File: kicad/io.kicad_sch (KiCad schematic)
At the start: 12 parts, among them J2 UART, P1 Mini-DIN_6pins_ver3, U13 uSD adapter, U14 8259, U16 16550, U17 T6963C

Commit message: PS/2 with GAL - finally
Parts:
- removed R2: 10K, Resistor_THT:R_Axial_DIN0204_L3.6mm_D1.6mm_P7.62mm_Horizontal, symbol Device:R
- added BZ1: Buzzer, symbol Device:Buzzer
- added R2 (x2): 10K, Resistor_THT:R_Axial_DIN0204_L3.6mm_D1.6mm_P7.62mm_Horizontal, symbol Device:R
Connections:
- net GND: now also BZ1.2 (+), R2.1
- net INT1: now also U?.17 (PC3); no longer U?.14 (PC0)
- net MCB: now also U?.22 (PB4), R2.2; no longer U?.4 (PA0)
- net PS2CLK: now also U?.13 (PC4); no longer U?.16 (PC2)
- net PS2DATA: now also U?.4 (PA0); no longer U?.18 (PB0)
- net TIMERCLK: now also U?.18 (CLK2)
- net BUZEN: now reaches U?.16 (G2)
- net BUZEN: now also U?.18 (PB0)
- net BUZOUT: now reaches U?.17 (OUT2)
- net BUZOUT: now also R2.2
- new net: BZ1.1 (-), R2.1
- no-connect marks 42 -> 38
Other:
- note added: "Buzzer"
- note added: "IBF_{A}"
- note added: "INTR_{A}"
- note added: "IO"
- note added: "Port A control for mode 1 (strobed I/O)"
- note added: "Port B control for mode 1 (strobed I/O)"
- note added: "~{STB}_{A}"

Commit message: V0.3 WIP
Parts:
- added U20: ATF22V10, Package_DIP:DIP-24_W7.62mm_Socket, symbol my:ATF22V10
- BZ1: footprint (none) -> Buzzer_Beeper:Buzzer_TDK_PS1240P02BT_D12.2mm_H6.5mm
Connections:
- net +5V: now also U20.24 (VCC)
- net AD_{0}: now also U20.21 (O)
- net AD_{1}: now also U20.20 (O)
- net AD_{2}: now also U20.19 (O)
- net AD_{3}: now also U20.18 (O)
- net AD_{4}: now also U20.17 (O)
- net AD_{5}: now also U20.16 (O)
- net AD_{6}: now also U20.15 (O)
- net AD_{7}: now also U20.14 (O)
- net A_{0}: now also U20.3 (I)
- net GND: now also U20.12 (GND)
- net INT1: now also U20.23 (O); no longer U?.17 (PC3)
- net PS2CLK: now also U20.1 (CLK); no longer U?.13 (PC4)
- net PS2DATA: now also U20.2 (I); no longer U?.4 (PA0)
- net ~{RD}: now also U20.4 (I)
- net at U16.32 (~{RTS}): no longer U13.6 (~{CS})
- net at U16.33 (~{DTR}): no longer U13.5 (SCK)
- net at U16.34 (~{OUT1}): no longer U13.4 (MOSI)
- net at U16.36 (~{CTS}): no longer U13.3 (MISO)
- net at U?.11 (PC6): now also U13.6 (~{CS})
- net at U?.12 (PC5): now also U13.5 (SCK)
- net at U?.14 (PC0): now also U13.3 (MISO)
- net SPKREN: now reaches U?.19 (PB1)
- net BUZEN renamed T2GATE
- net BUZOUT renamed SPKROUT
- net SPKROUT: no longer U?.17 (OUT2)
- new net: U13.4 (MOSI), U?.13 (PC4)
- new net PS2~{EN}: U20.13 (I)
- new net T2OUT: U?.17 (OUT2)
- no-connect marks 38 -> 48
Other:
- note added: "Mode = 0 (basic)"
- note added: "Peripheral controller"
- note added: "Port A = N/C"
- note added: "Port B = 0 (OUT)"
- note added: "Port C (high) = 0 (OUT)"
- note added: "Port C (low) = 1 (IN)"
- note added: "Speaker"
- note removed: "0,1"
- note removed: "Buzzer"
- note removed: "IBF_{A}"
- note removed: "IBF_{B}"
- note removed: "INTR_{A}"
- note removed: "INTR_{B}"
- note removed: "IO"
- note removed: "Mode = 1 (strobe)"
- note removed: "PC_{2} <- 1 (enable interrupts on Group B)"
- note removed: "Port A = IN & OUT"
- note removed: "Port A control for mode 1 (strobed I/O)"
- note removed: "Port B = INPUT"
- note removed: "Port B control for mode 1 (strobed I/O)"
- note removed: "Port C (high) = OUTPUT"
- note removed: "Port C (low) = N/C"
- note removed: "~{STB}_{A}"
- note removed: "~{STB}_{B}"
- moved on the sheet: U13

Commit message: WIP: PCB v3.0
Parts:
- renumbered U20 to KB1, U17 to LCD1, U14 to PIC1, U13 to SD1, U16 to UART1
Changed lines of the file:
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@@
   (symbol (lib_id "82xx:16550") (at 73.66 144.78 0) (unit 1)
     (in_bom yes) (on_board yes) (dnp no) (fields_autoplaced)
-    (property "Reference" "U16" (at 75.8541 107.95 0)
+    (property "Reference" "UART1" (at 75.8541 107.95 0)
       (effects (font (size 1.27 1.27)) (justify left))
     )
@@
       (project "main"
         (path "/590a4a95-7c0e-40dd-8637-8ee29cb6972a/3a7ee20c-9aab-4bcf-8400-2397304f0b30"
-          (reference "U16") (unit 1)
+          (reference "UART1") (unit 1)
         )
       )
@@
   (symbol (lib_id "my:ATF22V10") (at 334.01 171.45 0) (unit 1)
     (in_bom yes) (on_board yes) (dnp no) (fields_autoplaced)
-    (property "Reference" "U20" (at 336.2041 154.94 0)
+    (property "Reference" "KB1" (at 336.2041 154.94 0)
       (effects (font (size 1.27 1.27)) (justify left))
     )
@@
       (project "main"
         (path "/590a4a95-7c0e-40dd-8637-8ee29cb6972a/3a7ee20c-9aab-4bcf-8400-2397304f0b30"
-          (reference "U20") (unit 1)
+          (reference "KB1") (unit 1)
         )
       )
@@
         )
         (path "/590a4a95-7c0e-40dd-8637-8ee29cb6972a/3a7ee20c-9aab-4bcf-8400-2397304f0b30"
-          (reference "U9") (unit 1)
+          (reference "PIT1") (unit 1)
         )
       )
@@
         )
         (path "/590a4a95-7c0e-40dd-8637-8ee29cb6972a/3a7ee20c-9aab-4bcf-8400-2397304f0b30"
-          (reference "U12") (unit 1)
+          (reference "PPI1") (unit 1)
         )
       )
@@
   (symbol (lib_id "my:uSD-adapter") (at 269.24 105.41 0) (unit 1)
     (in_bom yes) (on_board yes) (dnp no) (fields_autoplaced)
-    (property "Reference" "U13" (at 279.4 104.14 0)
+    (property "Reference" "SD1" (at 279.4 104.14 0)
       (effects (font (size 1.27 1.27)) (justify left))
     )
@@
       (project "main"
         (path "/590a4a95-7c0e-40dd-8637-8ee29cb6972a/3a7ee20c-9aab-4bcf-8400-2397304f0b30"
-          (reference "U13") (unit 1)
+          (reference "SD1") (unit 1)
         )
       )
@@
   (symbol (lib_id "Interface:8259") (at 74.93 58.42 0) (unit 1)
     (in_bom yes) (on_board yes) (dnp no) (fields_autoplaced)
-    (property "Reference" "U14" (at 77.1241 29.845 0)
-      (effects (font (size 1.27 1.27)) (justify left))
-    )
-    (property "Value" "8259" (at 77.1241 32.385 0)
+    (property "Reference" "PIC1" (at 77.1241 29.21 0)
+      (effects (font (size 1.27 1.27)) (justify left))
+    )
+    (property "Value" "8259" (at 77.1241 31.75 0)
       (effects (font (size 1.27 1.27)) (justify left))
     )
@@
       (project "main"
         (path "/590a4a95-7c0e-40dd-8637-8ee29cb6972a/3a7ee20c-9aab-4bcf-8400-2397304f0b30"
-          (reference "U14") (unit 1)
+          (reference "PIC1") (unit 1)
         )
       )
@@
   (symbol (lib_id "lcd:24064-LCD") (at 177.8 185.42 0) (unit 1)
     (in_bom yes) (on_board yes) (dnp no) (fields_autoplaced)
-    (property "Reference" "U17" (at 182.5341 210.82 0)
-      (effects (font (size 1.27 1.27)) (justify left))
-    )
-    (property "Value" "T6963C" (at 182.5341 213.36 0)
-      (effects (font (size 1.27 1.27)) (justify left))
+    (property "Reference" "LCD1" (at 193.04 159.4419 0)
+      (effects (font (size 1.27 1.27)))
+    )
+    (property "Value" "T6963C" (at 193.04 161.9819 0)
+      (effects (font (size 1.27 1.27)))
     )
     (property "Footprint" "footprints:LCD24064" (at 177.8 160.02 0)
@@
       (project "main"
         (path "/590a4a95-7c0e-40dd-8637-8ee29cb6972a/3a7ee20c-9aab-4bcf-8400-2397304f0b30"
-          (reference "U17") (unit 1)
-        )
-      )
+          (reference "LCD1") (unit 1)
+        )
+      )

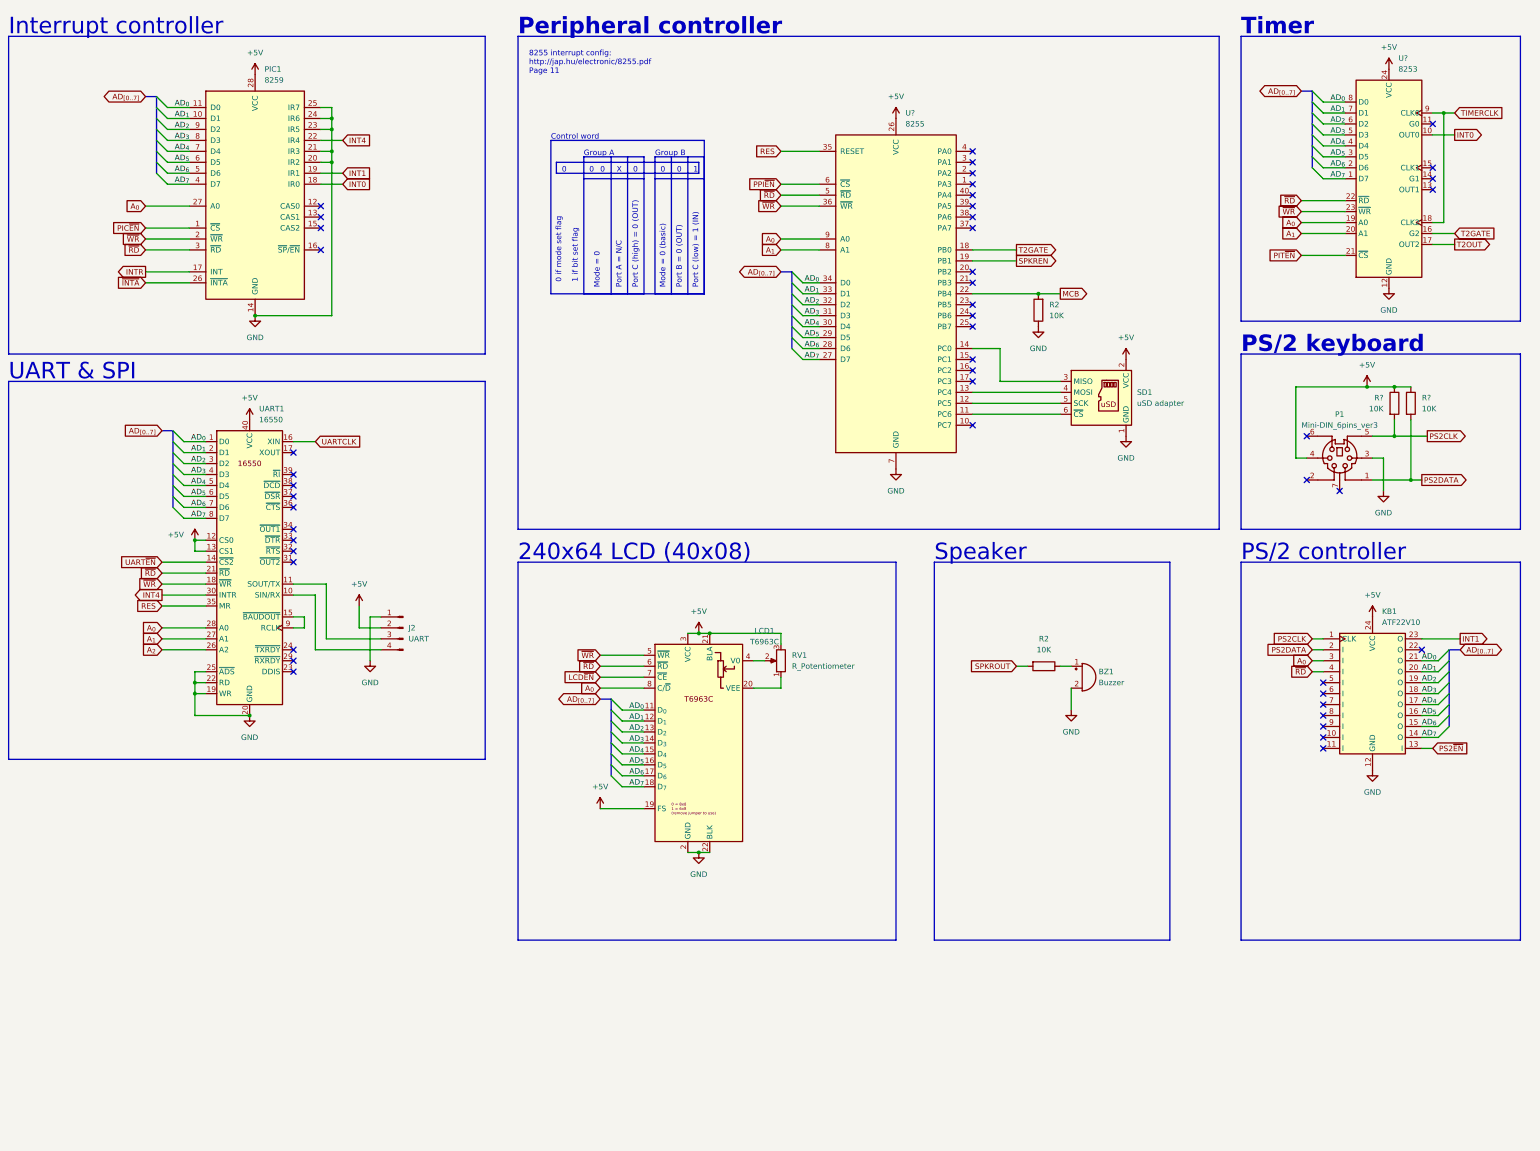
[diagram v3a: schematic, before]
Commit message: Add SPI controller to PCB v0.3
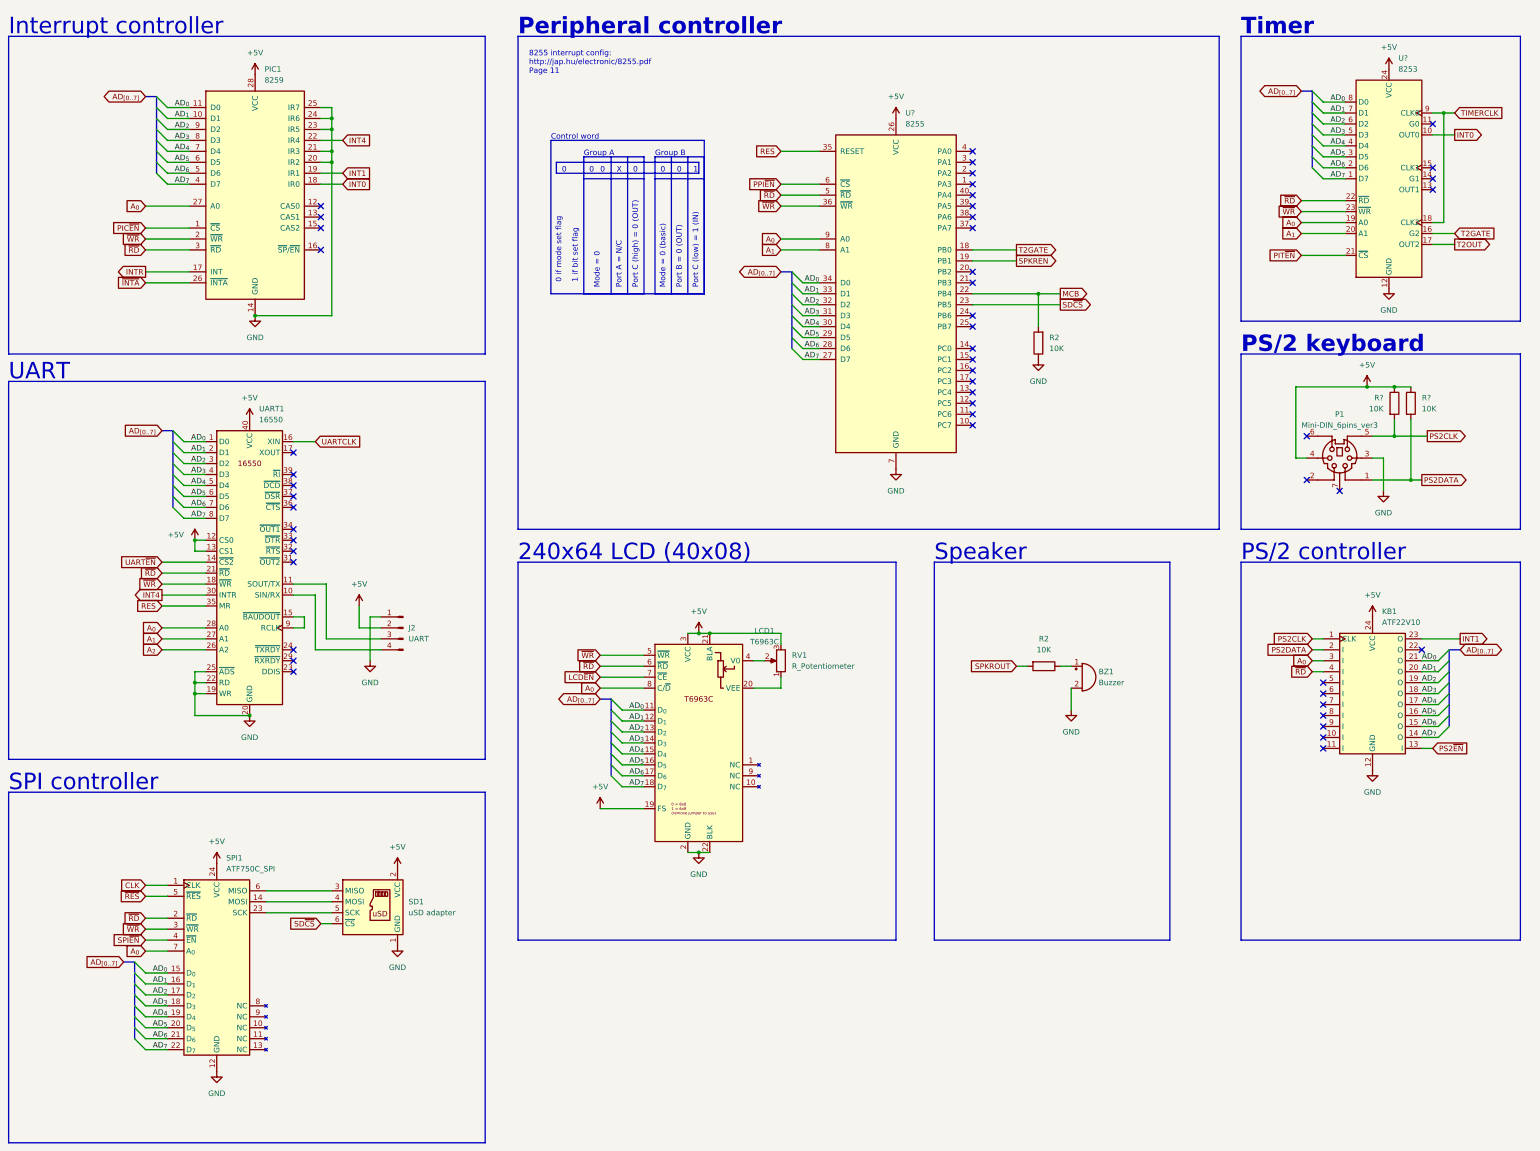
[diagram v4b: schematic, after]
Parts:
- added SPI1: ATF750C_SPI, Package_DIP:DIP-24_W7.62mm_Socket, symbol my:ATF750C_SPI
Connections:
- net +5V: now also SPI1.24 (VCC)
- net AD_{0}: now also SPI1.15 (D_{0})
- net AD_{1}: now also SPI1.16 (D_{1})
- net AD_{2}: now also SPI1.17 (D_{2})
- net AD_{3}: now also SPI1.18 (D_{3})
- net AD_{4}: now also SPI1.19 (D_{4})
- net AD_{5}: now also SPI1.20 (D_{5})
- net AD_{6}: now also SPI1.21 (D_{6})
- net AD_{7}: now also SPI1.22 (D_{7})
- net A_{0}: now also SPI1.7 (A_{0})
- net GND: now also SPI1.12 (GND)
- net ~{RD}: now also SPI1.2 (~{RD})
- net ~{WR}: now also SPI1.3 (~{WR})
- net at U?.11 (PC6): no longer SD1.6 (~{CS})
- net at SD1.5 (SCK): now also SPI1.23 (SCK); no longer U?.12 (PC5)
- net at SD1.4 (MOSI): now also SPI1.14 (MOSI); no longer U?.13 (PC4)
- net at SD1.3 (MISO): now also SPI1.6 (MISO); no longer U?.14 (PC0)
- net SD~{CS}: now reaches U?.23 (PB5)
- net SD~{CS}: now also SD1.6 (~{CS})
- new net CLK: SPI1.1 (CLK)
- new net SPI~{EN}: SPI1.4 (~{EN})
- new net ~{RES}: SPI1.5 (~{RES})
- no-connect marks 48 -> 51
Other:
- note added: "SPI controller"
- note added: "UART"
- note removed: "UART & SPI"
- moved on the sheet: R2

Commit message: WIP - PCB v0.4
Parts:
- LCD1: footprint footprints:LCD24064 -> footprints:LCD240128_TFT_var2
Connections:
- net AD_{0}: now also KB1.15 (O); no longer KB1.21 (O)
- net AD_{1}: now also KB1.16 (O); no longer KB1.20 (O)
- net AD_{2}: now also KB1.17 (O); no longer KB1.19 (O)
- net AD_{4}: now also KB1.19 (O); no longer KB1.17 (O)
- net AD_{5}: now also KB1.20 (O); no longer KB1.16 (O)
- net AD_{6}: now also KB1.21 (O); no longer KB1.15 (O)
- net AD_{7}: now also KB1.22 (O); no longer KB1.14 (O)
